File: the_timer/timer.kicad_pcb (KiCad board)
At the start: 2 copper layers, 18 x 34 mm, 17 parts, among them J1 AVR-ISP-6, J2 Conn_01x05_Socket, Q1 2N7002, Q2 2N7002, Q3 2N7002, Q4 2N7002, U1 ATtiny48-A, U2 TPS61033, U3 MC3416

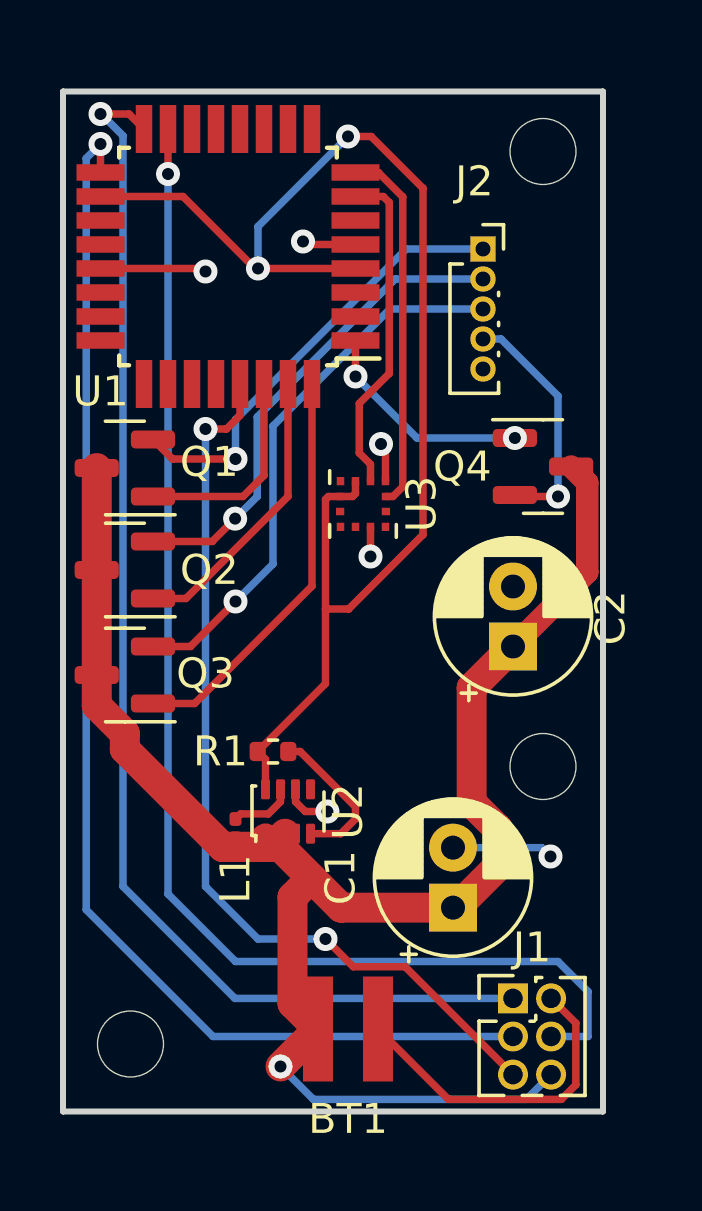
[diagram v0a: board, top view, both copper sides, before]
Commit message: added memory to the timer
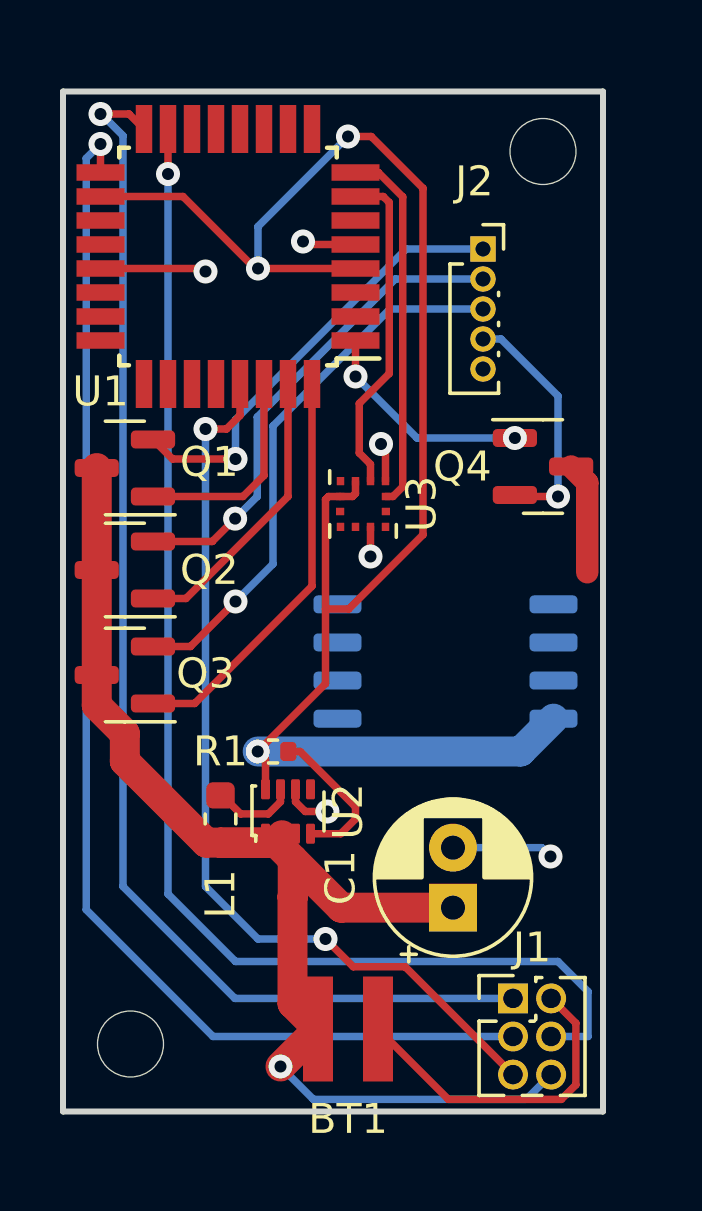
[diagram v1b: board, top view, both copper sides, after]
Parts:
- removed C2: 220u, Capacitor_THT:CP_Radial_D5.0mm_P2.00mm
- removed the REF** at (222.0, 97.2)
- added U4: W25Q128JVS, Package_SO:SOIC-8_5.23x5.23mm_P1.27mm, B.Cu at (218.8, 93.8)
- L1: value 200nH -> 0.47u; footprint Inductor_SMD:L_0201_0603Metric -> Inductor_SMD:L_0603_1608Metric
- R1: value R_Small_US -> 0
- moved L1 0.59 mm to (211.2, 99.0)
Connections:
- U1 pad 14: unconnected-(U1-PB2-Pad14) -> FCS
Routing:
- net V_{cc}: track 62.4 -> 47.7 mm
- net V_{reg}: track 46.4 -> 56.7 mm, vias 2 -> 3
- net Net-(U2-SW): track 2.15 -> 2.84 mm

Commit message: Finished rerouting timer
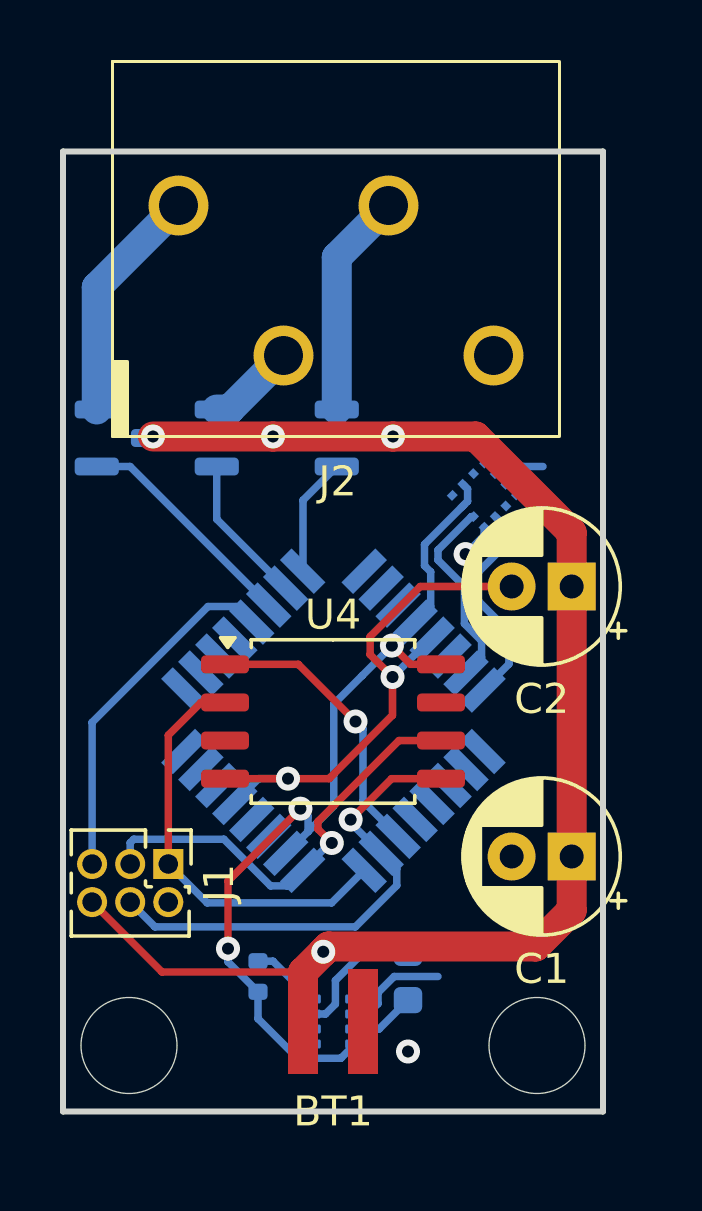
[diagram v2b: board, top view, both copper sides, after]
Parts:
- removed Q4: 2N7002, Package_TO_SOT_SMD:SOT-23
- removed the REF** at (222.0, 76.8)
- removed the REF** at (208.2, 106.5)
- added C2: 220u, Capacitor_THT:CP_Radial_D5.0mm_P2.00mm, F.Cu at (223.0, 91.2)
- added REF**: MountingHole_3.2mm_M3, MountingHole:MountingHole_3.2mm_M3, F.Cu at (208.2, 106.5)
- added REF**: MountingHole_3.2mm_M3, MountingHole:MountingHole_3.2mm_M3, F.Cu at (221.8, 106.5)
- BT1: footprint kifootprints:TE Right Angle JST -> locals:TE Right Angle JST
- J2: value Conn_01x05_Socket -> Conn_01x04_Socket; footprint Connector_PinSocket_1.00mm:PinSocket_1x05_P1.00mm_Vertical -> locals:TE_1-2834019-4
- L1, Q1, Q2, Q3, R1, U1, U2, U3: moved to B.Cu
- U4: moved to F.Cu
- moved U1 15.9 mm to (215.0, 95.7), turned to -135 degrees
- moved J2 13.8 mm to (207.7, 86.2)
- moved J1 12.3 mm to (209.5, 100.5), turned to -90 degrees
- moved Q3 11.2 mm to (216.1, 86.3), turned to 0 degrees
- moved L1 8.16 mm to (217.5, 104.2), turned to 90 degrees
- moved R1 7.52 mm to (212.5, 104.2), turned to -90 degrees
- moved U2 7.16 mm to (215.0, 105.8), turned to 0 degrees
- moved Q2 5.95 mm to (212.1, 86.3), turned to 0 degrees
- moved C1 4.31 mm to (223.0, 100.2), turned to 180 degrees
- moved U4 4.25 mm to (215.0, 95.8)
- moved U3 4.06 mm to (220.0, 88.2), turned to 45 degrees
- moved Q1 1.00 mm to (208.1, 86.3), turned to 0 degrees
- moved BT1 0.56 mm to (214.0, 105.8)
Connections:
- J2 pad 4: c3 -> GND
- U1 pad 1: t3 -> unconnected-(U1-PD3-Pad1)
- U4 pad 1: unconnected-(U4-~{CS}-Pad1) -> FCS
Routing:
- net MISO: track 42.3 -> 14.2 mm, vias 1 -> 0
- net SCK: track 42.6 -> 14.8 mm
- net MOSI: track 43.6 -> 16.2 mm
- net V_{reg}: track 56.7 -> 30.2 mm
- net ~{RESET}: track 30.5 -> 11.9 mm, vias 2 -> 0
- net c1: track 16.2 -> 2.97 mm, vias 1 -> 0
- net c2: track 18.4 -> 7.51 mm, vias 1 -> 0
- net t2: track 13.7 -> 3.97 mm
- net FCS: track 0.00 -> 9.56 mm, vias 0 -> 1
- net c3: track 8.10 -> 0.00 mm, vias 1 -> 0
- net t3: track 7.36 -> 0.00 mm, vias 2 -> 0
- net c0: track 14.9 -> 7.93 mm, vias 1 -> 0
- net V_{cc}: track 47.7 -> 54.2 mm, vias 1 -> 4
- net SCL: track 12.3 -> 6.92 mm
- net t1: track 9.66 -> 5.02 mm
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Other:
- board size 18 x 34 mm -> 18 x 32 mm
